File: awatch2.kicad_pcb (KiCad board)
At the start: 4 copper layers, 73.4 x 64.4 mm, 169 parts, among them J101 Conn_01x02, J102 Conn_01x02, J103 Conn_01x02, J104 Conn_01x02, J301 Conn_01x02, J801 Molex 1050170001, J802 Conn_01x06, Q701 FDV301N, SW101 B3S-1000, SW102 B3S-1000, SW103 B3S-1000, SW104 B3S-1000, U1 nRF52840, U301 MAX14690, U401 W25Q128JVPIQTR, U501 BMM150, U502 APDS-9306-065, U503 BMI160, U504 BMP388, U601 SPK0641HT4H-1, U701 AYF531035 (LS013B7DH05), U801 AT93C46DN-SH-T, U802 MCP1703A-3302_SOT223, U803 FT2232HL, U901 DRV2604, X1 ABM11W-32.0000MHZ-8-B1U-T3, Y801 FH1200004

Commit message: update solder mask clearance for oshpark
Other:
- rule pad_to_mask_clearance: 0.051 -> 0.0381
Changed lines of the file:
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@@
     (pad_size 1.524 1.524)
     (pad_drill 0.762)
-    (pad_to_mask_clearance 0.051)
-    (solder_mask_min_width 0.25)
+    (pad_to_mask_clearance 0.0381)
     (aux_axis_origin 0 0)
     (visible_elements FFFFF77F)
@@
       (outputformat 1)
       (mirror false)
-      (drillshape 1)
+      (drillshape 0)
       (scaleselection 1)
-      (outputdirectory ""))
+      (outputdirectory "gerber_out/"))
   )
   (net 0 "")

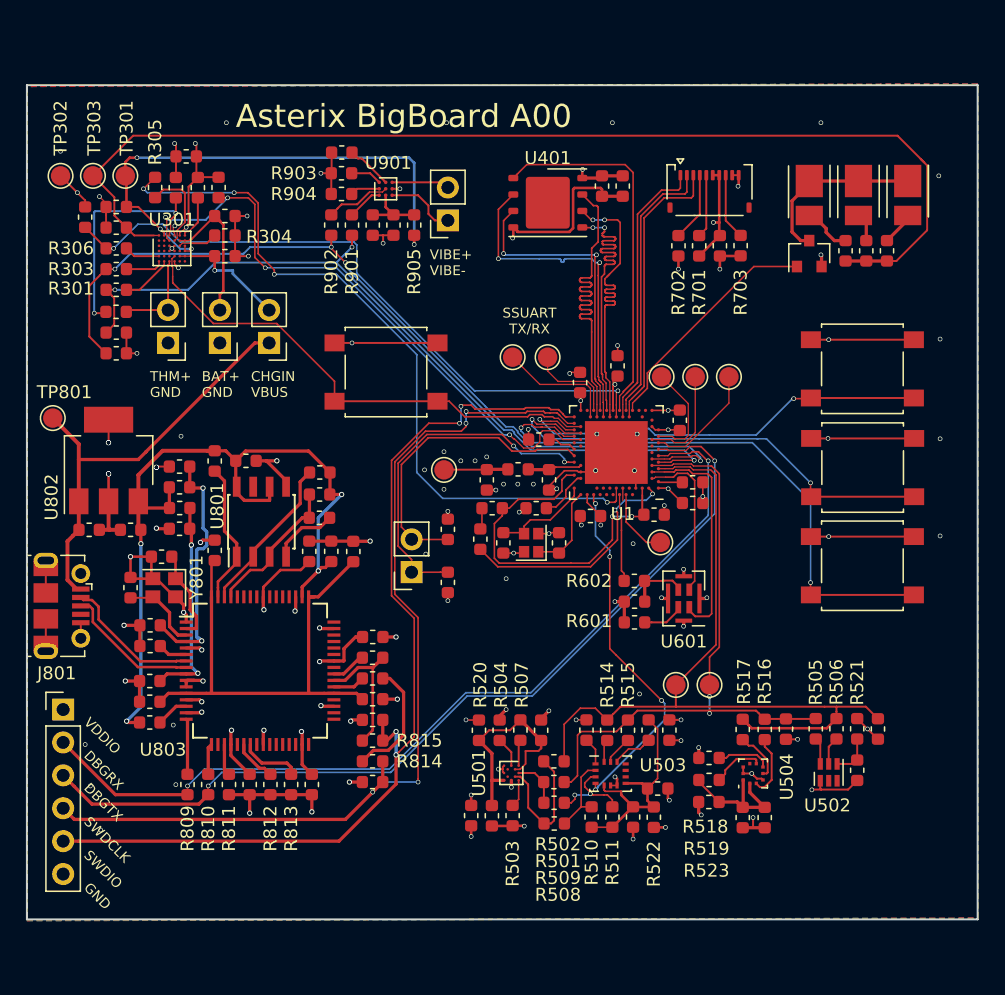
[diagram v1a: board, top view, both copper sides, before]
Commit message: mounting holes, fiducials
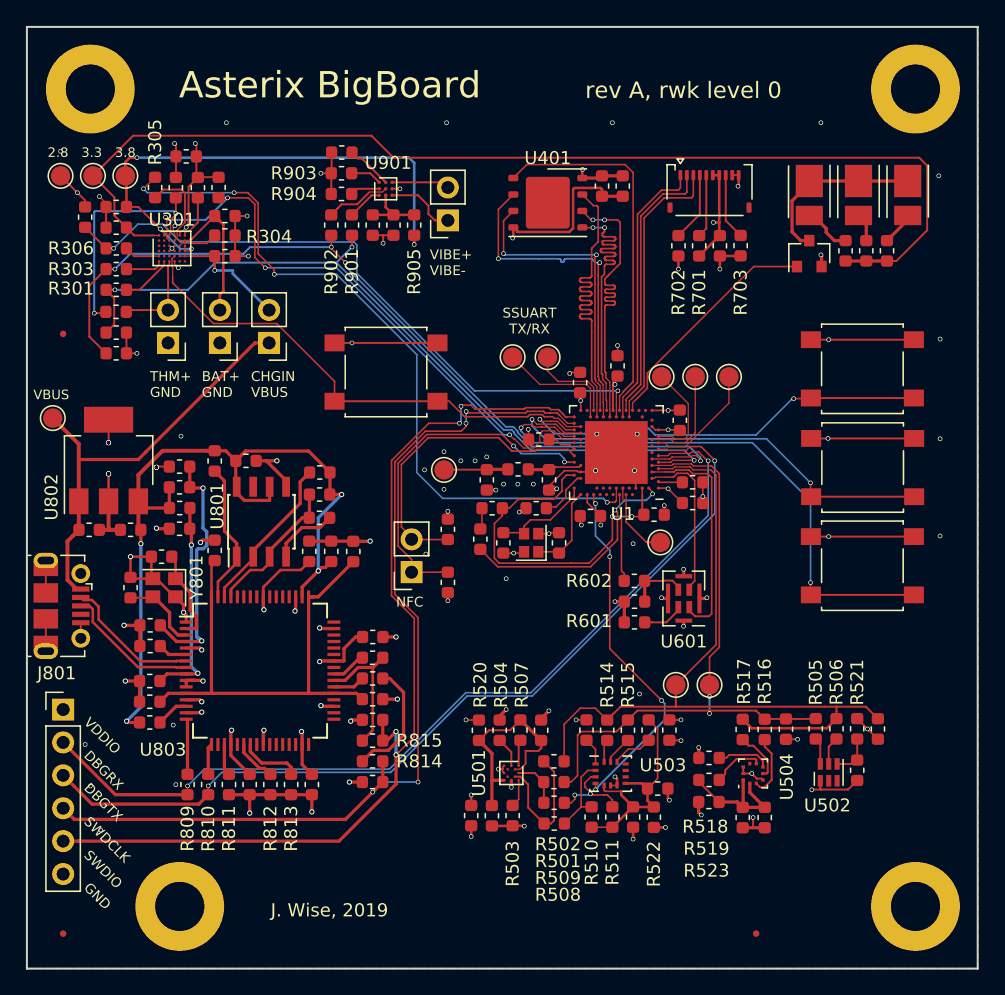
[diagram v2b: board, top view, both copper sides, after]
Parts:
- added REF**: Fiducial_0.5mm_Dia_1mm_Outer, Fiducial:Fiducial_0.5mm_Dia_1mm_Outer, F.Cu at (100.3, 96.0)
- added REF**: Fiducial_0.5mm_Dia_1mm_Outer, Fiducial:Fiducial_0.5mm_Dia_1mm_Outer, F.Cu at (46.8, 49.7)
- added REF**: 6-32, awatch2-footprints:6-32, F.Cu at (112.1, 30.7)
- added REF**: 6-32, awatch2-footprints:6-32, F.Cu at (48.9, 30.7)
- added REF**: 6-32, awatch2-footprints:6-32, F.Cu at (112.6, 93.8)
- added REF**: 6-32, awatch2-footprints:6-32, F.Cu at (55.8, 93.9)
- added REF**: Fiducial_0.5mm_Dia_1mm_Outer, Fiducial:Fiducial_0.5mm_Dia_1mm_Outer, F.Cu at (46.8, 96.0)
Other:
- board size 73.4 x 64.4 mm -> 73.4 x 72.7 mm
- board text added: "2.8"
- board text added: "3.3"
- board text added: "3.8"
- board text added: "Asterix BigBoard"
- board text added: "J. Wise, 2019"
- board text added: "NFC"
- board text added: "VBUS"
- board text added: "rev A, rwk level 0"
- board text removed: "Asterix BigBoard A00"

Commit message: oops, connect the rest of the grounds
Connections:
- REF** pad GND: (no net) -> GND (x3)
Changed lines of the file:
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@@
     )
     (pad GND thru_hole circle (at 0.5 0.1) (size 6.858 6.858) (drill 3.7973) (layers *.Cu *.Mask)
-      (zone_connect 2))
+      (net 3 GND) (zone_connect 2))
   )
   (module awatch2-footprints:6-32 (layer F.Cu)
@@
     )
     (pad GND thru_hole circle (at 0 0.1) (size 6.858 6.858) (drill 3.7973) (layers *.Cu *.Mask)
-      (zone_connect 2))
+      (net 3 GND) (zone_connect 2))
   )
   (module awatch2-footprints:6-32 (layer F.Cu)
@@
     (fp_circle (center 0 0) (end 2.5 0) (layer F.CrtYd) (width 0.05))
     (pad GND thru_hole circle (at 0 0.1) (size 6.858 6.858) (drill 3.7973) (layers *.Cu *.Mask)
-      (zone_connect 2))
+      (net 3 GND) (zone_connect 2))
   )
   (module Capacitor_SMD:C_0603_1608Metric (layer F.Cu)

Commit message: approx. final layout
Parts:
- removed REF** (x2): 6-32, awatch2-footprints:6-32
- added G1: Logo, awatch2-footprints:littlehatguy, B.Cu at (83.5, 79.2)
- added H1001: 6-32, awatch2-footprints:6-32, F.Cu at (48.9, 30.7)
- added H1002: 6-32, awatch2-footprints:6-32, F.Cu at (112.1, 30.7)
- C12, C5, C7, C8: value 100nF X7R -> 0.1µF X7R
- C301, C302, C303, C306, C401, C501, C504, C701, C901, C903: value 1µF -> 1.0µF X7R
- C402, C902: value 0.1µF -> 0.1µF X7R
- C502, C503, C505, C506, C507, C508, C601, C801, C802, C803, C809, C810, C811, C812, C813, C814, C815, C816, C817, C818: value .1µF -> 0.1µF X7R
- C804, C806: value 4.7µF -> 4.7µF X7R
- C805, C807: value 22pF -> 22pF NP0
- C808: value 3.3µF -> 4.7µF X7R
- H1005, H1006, H1007: renamed from REF**; value Fiducial_0.5mm_Dia_1mm_Outer -> Fiducial
- J101, J104: footprint Connector_PinSocket_2.54mm:PinSocket_1x02_P2.54mm_Vertical -> Connector_PinHeader_2.54mm:PinHeader_1x02_P2.54mm_Vertical
- U301: value MAX14690 -> MAX14690A
- moved R703 5.95 mm to (93.2, 42.7)
- moved R702 3.66 mm to (98.0, 42.7)
- moved C701 2.76 mm to (94.8, 42.7)
- moved R701 0.50 mm to (96.3, 42.7)
- renumbered REF** to H1003, REF** to H1004
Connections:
- U1 pad AC11: /Display/DISP_SCK -> /Display/DISP_CSN
- U1 pad AC9: /Display/DISP_CSN -> /Display/DISP_SCK
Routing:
- net /Display/DISP_SCK: track 21.3 -> 25.9 mm
- net /Display/DISP_MOSI: track 21.1 -> 25.4 mm
- net /Display/DISP_CSN: track 21.9 -> 26.1 mm
- net /Display/BL_PWM: track 18.3 -> 22.2 mm
- net Net-(R702-Pad1): track 5.35 -> 4.66 mm
- net GND: track 191.1 -> 190.5 mm, vias 114 -> 117
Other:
- board text added: "thanks: ajw, ginge, kevtris, sgstair, mrwright, j4cbo, Katharine, Tation, ishotjr, …"

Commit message: update values in pcb
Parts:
- R304: value 12.5k -> 12.4k
- R806: value 1k -> 2.2k
- R808: value 50 -> 160
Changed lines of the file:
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@@
       (effects (font (size 1 1) (thickness 0.15)))
     )
-    (fp_text value 12.5k (at 0 1.43) (layer F.Fab)
+    (fp_text value 12.4k (at 0 1.43) (layer F.Fab)
       (effects (font (size 1 1) (thickness 0.15)))
     )
@@
       (effects (font (size 1 1) (thickness 0.15)))
     )
-    (fp_text value 1k (at 0 1.43) (layer F.Fab)
+    (fp_text value 2.2k (at 0 1.43) (layer F.Fab)
       (effects (font (size 1 1) (thickness 0.15)))
     )
@@
       (effects (font (size 1 1) (thickness 0.15)))
     )
-    (fp_text value 50 (at 0 1.43 180) (layer F.Fab)
+    (fp_text value 160 (at 0 1.43 180) (layer F.Fab)
       (effects (font (size 1 1) (thickness 0.15)))
     )
@@
       (xy -0.952028 8.605013)) (layer B.SilkS) (width 0.01))
   )
-  (gr_text "thanks:\najw, ginge, kevtris, sgstair, mrwright, j4cbo,\nKatharine, Tation, ishotjr, …" (at 83.5 93.2) (layer B.SilkS)
+  (gr_text "thanks:\najw, ginge, kevtris, sgstair, mrwright,\nj4cbo, Katharine, Tation, ishotjr, …" (at 83.5 93.2) (layer B.SilkS)
     (effects (font (size 1.016 1.016) (thickness 0.2032)) (justify mirror))
   )
